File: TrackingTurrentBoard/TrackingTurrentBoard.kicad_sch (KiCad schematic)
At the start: 0 parts

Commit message: added symbols and started power circuits
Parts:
- added U101: STM32L433CCTx, Package_QFP:LQFP-48_7x7mm_P0.5mm, symbol MCU_ST_STM32L4:STM32L433CCTx
- added U102: FT232RL, Package_SO:SSOP-28_5.3x10.2mm_P0.65mm, symbol Interface_USB:FT232RL
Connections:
- new net: U101.23 (VSS), U101.35 (VSS), U101.47 (VSS)
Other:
- added sheet Connectors (Connectors.kicad_sch)
- added sheet GPS (GPS.kicad_sch)
- added sheet Motors (Motors.kicad_sch)
- added sheet Power (Power.kicad_sch)
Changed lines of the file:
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@@
     (comment 4 "Engineers: Quinn Athas, Aidan Costello")
+  )
+  (symbol (lib_id "Interface_USB:FT232RL") (at 219.71 173.355 0) (unit 1)
+    (in_bom yes) (on_board yes) (dnp no) (fields_autoplaced)
+    (property "Reference" "U102" (at 224.4441 147.32 0)
+      (effects (font (size 1.27 1.27)) (justify left))
+    )
+    (property "Value" "FT232RL" (at 224.4441 149.86 0)
+      (effects (font (size 1.27 1.27)) (justify left))
+    )
+    (property "Footprint" "Package_SO:SSOP-28_5.3x10.2mm_P0.65mm" (at 247.65 196.215 0)
+      (effects (font (size 1.27 1.27)) hide)
+    )
+    (property "Datasheet" "https://www.ftdichip.com/Support/Documents/DataSheets/ICs/DS_FT232R.pdf" (at 219.71 173.355 0)
+      (effects (font (size 1.27 1.27)) hide)
+    )
+    (pin "1")
+    (pin "10")
+    (pin "11")
+    (pin "12")
+    (pin "13")
+    (pin "14")
+    (pin "15")
+    (pin "16")
+    (pin "17")
+    (pin "18")
+    (pin "19")
+    (pin "2")
+    (pin "20")
+    (pin "21")
+    (pin "22")
+    (pin "23")
+    (pin "25")
+    (pin "26")
+    (pin "27")
+    (pin "28")
+    (pin "3")
+    (pin "4")
+    (pin "5")
+    (pin "6")
+    (pin "7")
+    (pin "9")
+    (instances
+      (project "TrackingTurrentBoard"
+        (path "/646d2382-5207-4eb7-a10d-a00ee180c70e"
+          (reference "U102") (unit 1)
+        )
+      )
+    )
+  )
+  (symbol (lib_id "MCU_ST_STM32L4:STM32L433CCTx") (at 218.44 91.44 0) (unit 1)
+    (in_bom yes) (on_board yes) (dnp no) (fields_autoplaced)
+    (property "Reference" "U101" (at 223.1741 129.54 0)
+      (effects (font (size 1.27 1.27)) (justify left))
+    )
+    (property "Value" "STM32L433CCTx" (at 223.1741 132.08 0)
+      (effects (font (size 1.27 1.27)) (justify left))
+    )
+    (property "Footprint" "Package_QFP:LQFP-48_7x7mm_P0.5mm" (at 205.74 127 0)
+      (effects (font (size 1.27 1.27)) (justify right) hide)
+    )
+    (property "Datasheet" "https://www.st.com/resource/en/datasheet/stm32l433cc.pdf" (at 218.44 91.44 0)
+      (effects (font (size 1.27 1.27)) hide)
+    )
+    (pin "1")
+    (pin "10")
+    (pin "11")
+    (pin "12")
+    (pin "13")
+    (pin "14")
+    (pin "15")
+    (pin "16")
+    (pin "17")
+    (pin "18")
+    (pin "19")
+    (pin "2")
+    (pin "20")
+    (pin "21")
+    (pin "22")
+    (pin "23")
+    (pin "24")
+    (pin "25")
+    (pin "26")
+    (pin "27")
+    (pin "28")
+    (pin "29")
+    (pin "3")
+    (pin "30")
+    (pin "31")
+    (pin "32")
+    (pin "33")
+    (pin "34")
+    (pin "35")
+    (pin "36")
+    (pin "37")
+    (pin "38")
+    (pin "39")
+    (pin "4")
+    (pin "40")
+    (pin "41")
+    (pin "42")
+    (pin "43")
+    (pin "44")
+    (pin "45")
+    (pin "46")
+    (pin "47")
+    (pin "48")
+    (pin "5")
+    (pin "6")
+    (pin "7")
+    (pin "8")
+    (pin "9")
+    (instances
+      (project "TrackingTurrentBoard"
+        (path "/646d2382-5207-4eb7-a10d-a00ee180c70e"
+          (reference "U101") (unit 1)
+        )
+      )
+    )
+  )
+  (sheet (at 15.24 114.935) (size 52.705 40.64) (fields_autoplaced)
+    (stroke (width 0.1524) (type solid))
+    (fill (color 0 0 0 0.0000))
+    (property "Sheetname" "Power" (at 15.24 114.2234 0)
+      (effects (font (size 1.27 1.27)) (justify left bottom))
+    )
+    (property "Sheetfile" "Power.kicad_sch" (at 15.24 156.1596 0)
+      (effects (font (size 1.27 1.27)) (justify left top))
+    )
+    (instances
+      (project "TrackingTurrentBoard"
+        (path "/646d2382-5207-4eb7-a10d-a00ee180c70e" (page "2"))
+      )
+    )
+  )
+  (sheet (at 17.78 64.135) (size 52.705 40.64) (fields_autoplaced)
+    (stroke (width 0.1524) (type solid))
+    (fill (color 0 0 0 0.0000))
+    (property "Sheetname" "Connectors" (at 17.78 63.4234 0)
+      (effects (font (size 1.27 1.27)) (justify left bottom))
+    )
+    (property "Sheetfile" "Connectors.kicad_sch" (at 17.78 105.3596 0)
+      (effects (font (size 1.27 1.27)) (justify left top))
+    )
+    (instances
+      (project "TrackingTurrentBoard"
+        (path "/646d2382-5207-4eb7-a10d-a00ee180c70e" (page "5"))
+      )
+    )
+  )
+  (sheet (at 15.875 163.83) (size 46.99 34.29) (fields_autoplaced)
+    (stroke (width 0.1524) (type solid))
+    (fill (color 0 0 0 0.0000))
+    (property "Sheetname" "GPS" (at 15.875 163.1184 0)
+      (effects (font (size 1.27 1.27)) (justify left bottom))
+    )
+    (property "Sheetfile" "GPS.kicad_sch" (at 15.875 198.7046 0)
+      (effects (font (size 1.27 1.27)) (justify left top))
+    )
+    (instances
+      (project "TrackingTurrentBoard"
+        (path "/646d2382-5207-4eb7-a10d-a00ee180c70e" (page "3"))
+      )
+    )
+  )
+  (sheet (at 16.51 16.51) (size 59.69 39.37) (fields_autoplaced)
+    (stroke (width 0.1524) (type solid))
+    (fill (color 0 0 0 0.0000))
+    (property "Sheetname" "Motors" (at 16.51 15.7984 0)
+      (effects (font (size 1.27 1.27)) (justify left bottom))
+    )
+    (property "Sheetfile" "Motors.kicad_sch" (at 16.51 56.4646 0)
+      (effects (font (size 1.27 1.27)) (justify left top))
+    )
+    (instances
+      (project "TrackingTurrentBoard"
+        (path "/646d2382-5207-4eb7-a10d-a00ee180c70e" (page "4"))
+      )
+    )
   )
   (sheet_instances

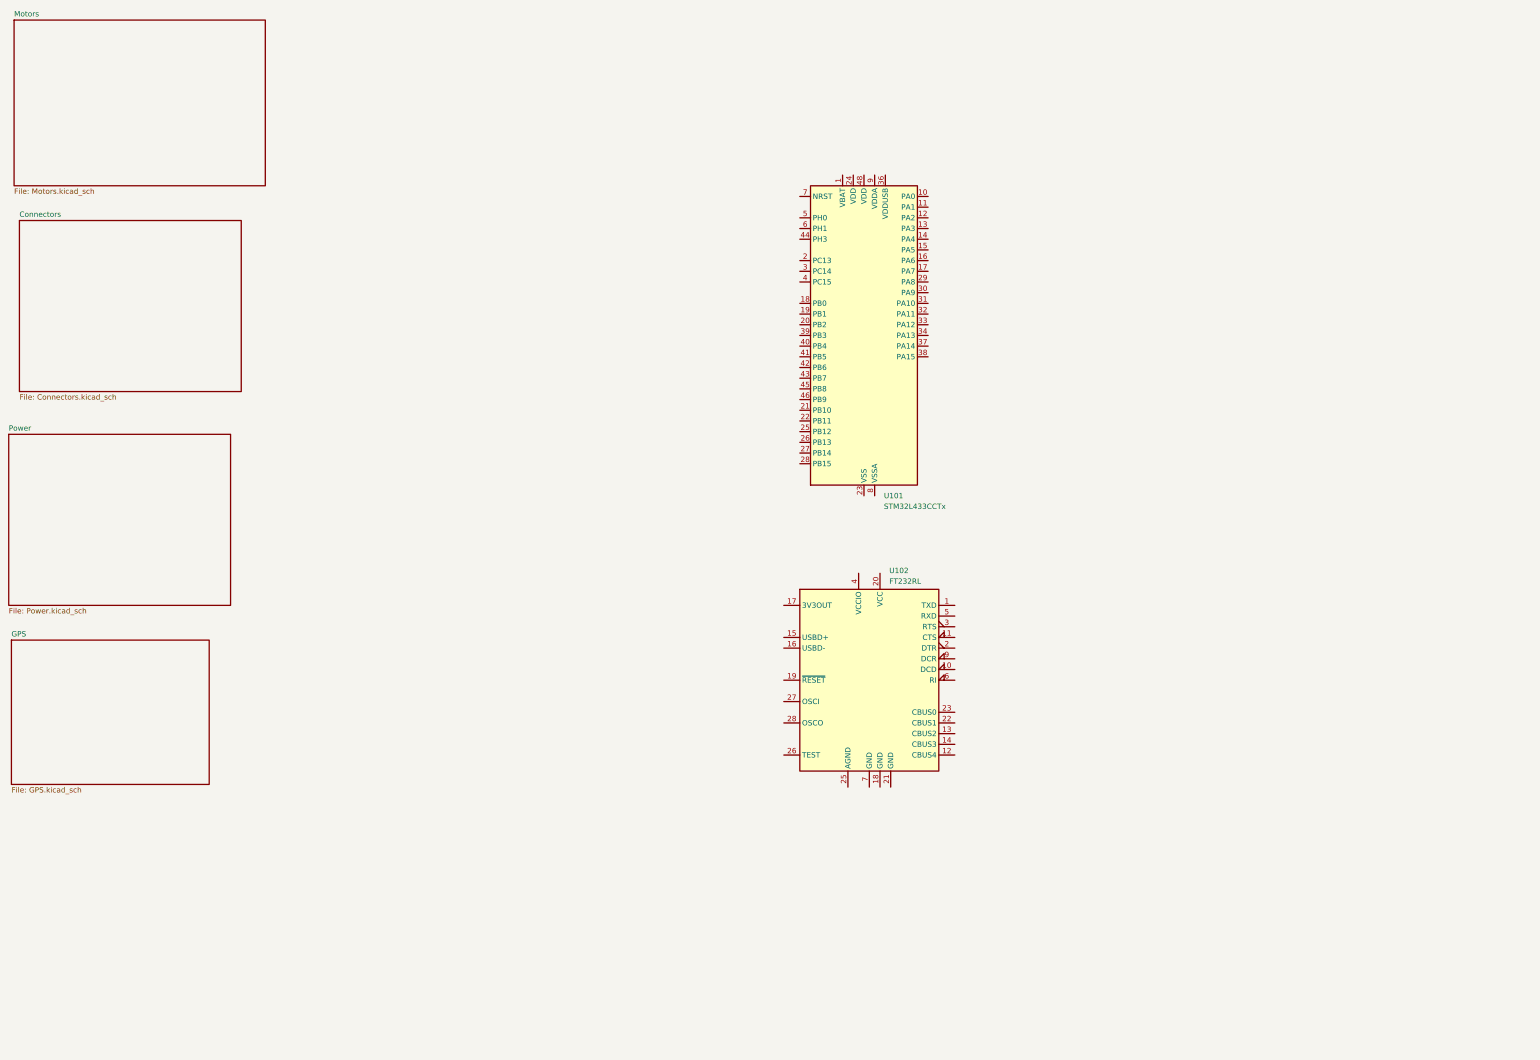
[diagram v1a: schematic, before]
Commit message: added buck sch
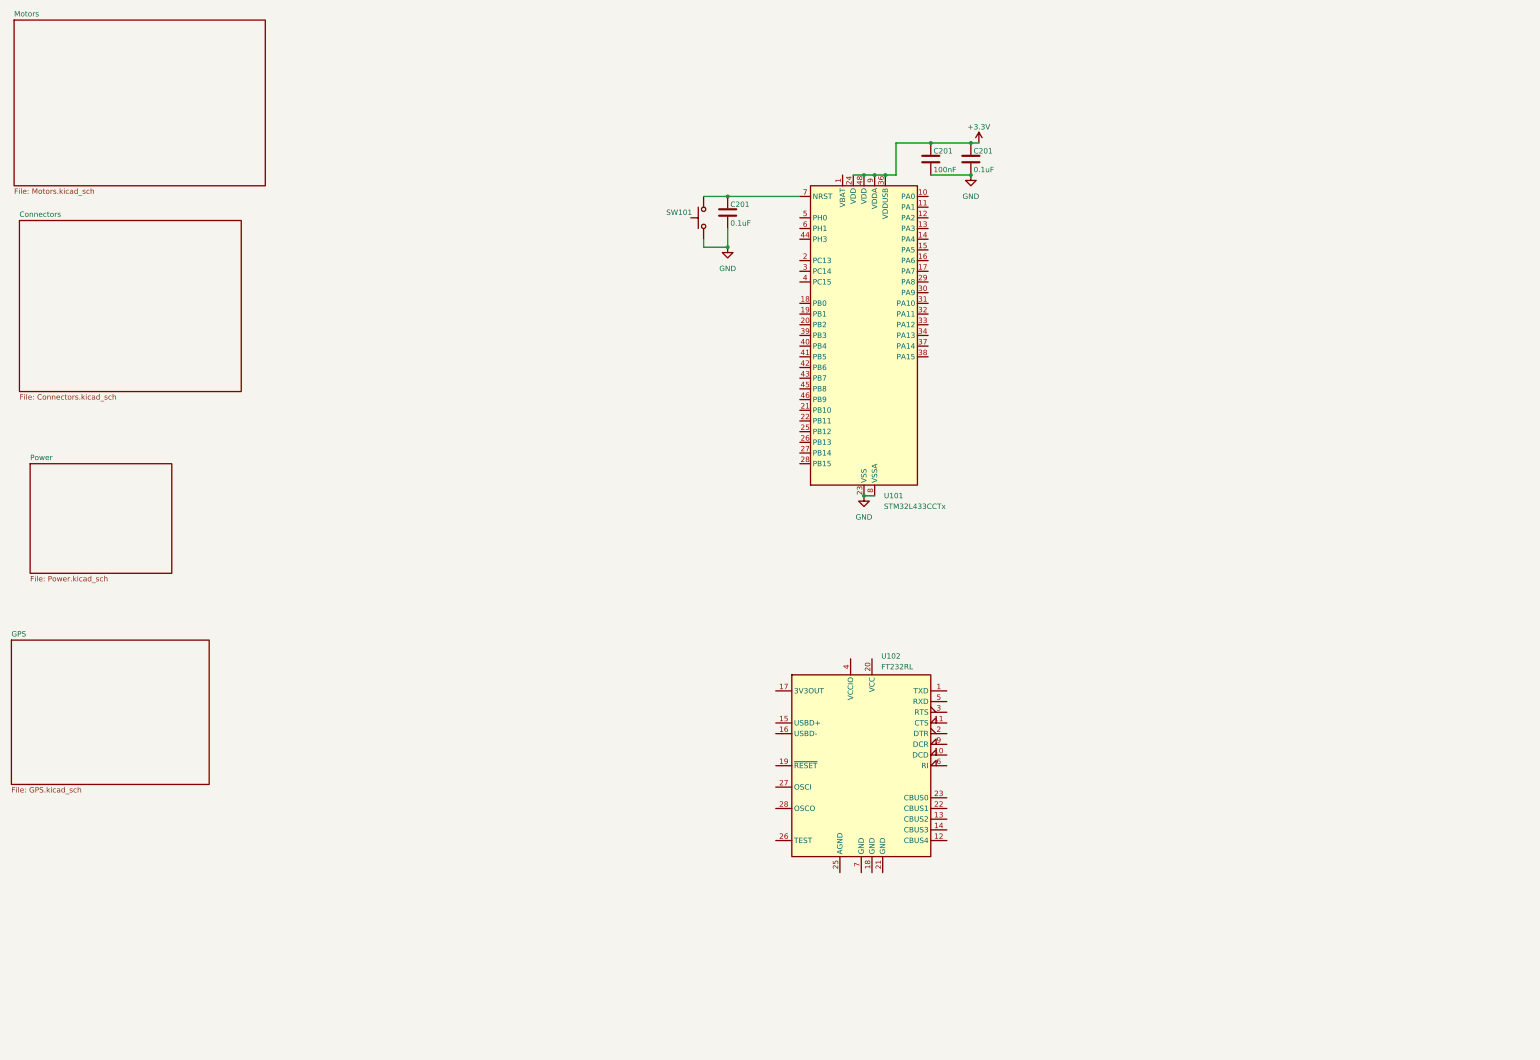
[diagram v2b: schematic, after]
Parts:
- added C201 (x2): 0.1uF, Capacitor_SMD:C_0603_1608Metric, symbol Device:C
- added C201: 100nF, Capacitor_SMD:C_0603_1608Metric, symbol Device:C
- added SW101: SW_MEC_5G, symbol Switch:SW_MEC_5G
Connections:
- net GND: now reaches U101.23 (VSS), U101.35 (VSS), U101.47 (VSS)
- net GND: now also U101.8 (VSSA), C201.2, C201.2, C201.2, SW101.1 (A), SW101.2 (A)
- net +3.3V: now reaches U101.24 (VDD)
- net +3.3V: now also U101.36 (VDDUSB), U101.48 (VDD), U101.9 (VDDA), C201.1, C201.1
- net at U101.7 (NRST): now also C201.1, SW101.3 (B), SW101.4 (B)
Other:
- moved on the sheet: U102

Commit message: PCB done
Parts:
- added C104, C105: 100nF, Capacitor_SMD:C_0603_1608Metric, symbol Device:C
- added C106: 4.7uF, Capacitor_SMD:C_0603_1608Metric, symbol Device:C
- added D101, D102, D103, D104, D105: LED, LED_SMD:LED_0603_1608Metric, symbol Device:LED
- added H101, H102, H103, H104: M4, MountingHole:MountingHole_4.3mm_M4_Pad_Via, symbol Mechanical:MountingHole_Pad
- added J101: Screw_Terminal_01x04, TerminalBlock_TE-Connectivity:TerminalBlock_TE_282834-4_1x04_P2.54mm_Horizontal, symbol Connector:Screw_Terminal_01x04
- added J102: Conn_01x05, Connector_PinHeader_2.54mm:PinHeader_1x05_P2.54mm_Vertical, symbol Connector_Generic:Conn_01x05
- added J103, J105, J106, J107: Conn_01x02, Connector_PinHeader_2.54mm:PinHeader_1x02_P2.54mm_Vertical, symbol Connector_Generic:Conn_01x02
- added J104: Conn_01x03, Connector_PinHeader_2.54mm:PinHeader_1x03_P2.54mm_Vertical, symbol Connector_Generic:Conn_01x03
- added J108: Screw_Terminal_01x02, TerminalBlock_TE-Connectivity:TerminalBlock_TE_282834-2_1x02_P2.54mm_Horizontal, symbol Connector:Screw_Terminal_01x02
- added J110: 2171790001, USB_Con:MOLEX_2171790001, symbol USB_Con:2171790001
- added R101, R102, R103, R106, R107: 100, Resistor_SMD:R_0603_1608Metric, symbol Device:R_US
- added R104, R105: 4.7k, Resistor_SMD:R_0603_1608Metric, symbol Device:R_US
- added R110, R111: 5.1k, Resistor_SMD:R_0603_1608Metric, symbol Device:R_US
- added U103: ECMF02-2AMX6, Package_DFN_QFN:ST_UQFN-6L_1.5x1.7mm_P0.5mm, symbol Power_Protection:ECMF02-2AMX6
- C103: renamed from C201; value 0.1uF -> 1uF
- SW101: footprint (none) -> Button_Switch_SMD:SW_SPST_CK_RS282G05A3
- renumbered C201 to C101, C201 to C102
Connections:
- net +3.3V: now also U101.1 (VBAT), J106.1 (Pin_1), R103.2, R104.2, R105.2
- net GND: now also U102.18 (GND), U102.21 (GND), U102.25 (AGND), U102.7 (GND), C104.2, C105.2, C106.2, D101.1 (K), D102.1 (K), D103.1 (K), D104.1 (K), D105.1 (K), H101.1, H102.1, H103.1, H104.1, J102.5 (Pin_5), J104.3 (Pin_3), J105.2 (Pin_2), J106.2 (Pin_2), J107.2 (Pin_2), J108.2 (Pin_2), J110.A1B12 (GND1), J110.B1A12 (GND2), J110.SH1 (SHIELD1), J110.SH2 (SHIELD2), J110.SH3 (SHIELD3), J110.SH4 (SHIELD4), R110.1, R111.2, U103.3 (GND), U103.4 (NC); no longer SW101.2 (A)
- net at C101.1, U101.7 (NRST): now also SW101.2 (B); no longer SW101.3 (B), SW101.4 (B)
- net FTDI_TX: now reaches U102.1 (TXD)
- net FTDI_TX: now also U101.21 (PB10)
- net FTDI_CTS: now reaches U102.11 (CTS)
- net FTDI_CTS: now also U101.26 (PB13)
- net USB_ESD+: now reaches U102.15 (USBD+)
- net USB_ESD+: now also U103.6 (D+_out)
- net USB_ESD-: now reaches U102.16 (USBD-)
- net USB_ESD-: now also U103.5 (D-_out)
- net at U102.17 (3V3OUT): now also C104.1
- net +5V: now reaches U102.20 (VCC)
- net +5V: now also U102.4 (VCCIO), C105.1, C106.1, J102.2 (Pin_2), J104.2 (Pin_2), J105.1 (Pin_1), R102.2
- net FTDI_RTS: now reaches U102.3 (RTS)
- net FTDI_RTS: now also U101.25 (PB12)
- net FTDI_RX: now reaches U102.5 (RXD)
- net FTDI_RX: now also U101.22 (PB11)
- net SERVO_PWM: now reaches U101.10 (PA0)
- net SERVO_PWM: now also J104.1 (Pin_1)
- net CHANNEL_B: now reaches U101.12 (PA2)
- net CHANNEL_B: now also J102.1 (Pin_1)
- net CHANNEL_A: now reaches U101.13 (PA3)
- net CHANNEL_A: now also J102.3 (Pin_3)
- net INDEX: now reaches U101.14 (PA4)
- net INDEX: now also J102.4 (Pin_4)
- net MODE3: now reaches U101.15 (PA5)
- net MODE2: now reaches U101.16 (PA6)
- net MODE1: now reaches U101.17 (PA7)
- net DIR: now reaches U101.18 (PB0)
- net STCK: now reaches U101.19 (PB1)
- net LED1: now reaches U101.2 (PC13)
- net LED1: now also R101.2
- net DECAY: now reaches U101.20 (PB2)
- net STEP_PWM: now reaches U101.29 (PA8)
- net LED2: now reaches U101.3 (PC14)
- net LED2: now also R106.2
- net EN\FAULT: now reaches U101.32 (PA11)
- net STBY\RST: now reaches U101.33 (PA12)
- net LED3: now reaches U101.4 (PC15)
- net LED3: now also R107.2
- net SCL: now reaches U101.42 (PB6)
- net SCL: now also J103.2 (Pin_2), R104.1
- net SDA: now reaches U101.43 (PB7)
- net SDA: now also J103.1 (Pin_1), R105.1
- net GPS_INT: now reaches U101.45 (PB8)
- net GPS_RST: now reaches U101.46 (PB9)
- new net: D101.2 (A), R101.1
- new net: J110.B5 (CC2), R111.1
- new net: D103.2 (A), R103.1
- new net: D102.2 (A), R102.1
- new net: D105.2 (A), R107.1
- new net: J110.A5 (CC1), R110.2
- new net: D104.2 (A), R106.1
- new net Motors/OUTA1: J101.1 (Pin_1)
- new net Motors/OUTA2: J101.2 (Pin_2)
- new net Motors/OUTB1: J101.3 (Pin_3)
- new net Motors/OUTB2: J101.4 (Pin_4)
- new net USB+: J110.A6 (DP1), J110.B6 (DP2), U103.1 (D+_in)
- new net USB-: J110.A7 (DN1), J110.B7 (DN2), U103.2 (D-_in)
- new net VBUS: J107.1 (Pin_1), J108.1 (Pin_1)
- no-connect marks 0 -> 30
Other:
- removed sheet Connectors
- sheet GPS ports: added GPS_INT, GPS_RST, SCL, SDA; removed none
- sheet Motors ports: added DECAY, DIR, EN\FAULT, MODE1, MODE2, MODE3, OUTA1, OUTA2, OUTB1, OUTB2, STBY\RST, STCK, STEP_PWM; removed none
- note added: "BLUE"
- note added: "GREEN"
- note added: "RED"
- note added: "Rotary Encoder Connector"
- note added: "Servo Motor Connector"
- note added: "Stepper Motor Outputs"
- note added: "USB Connector and Translator"
- moved on the sheet: U102
